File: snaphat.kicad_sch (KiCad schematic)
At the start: 98 parts, among them J1 Conn_01x08_S8B-PH-K-S(LF)(SN), J10 P70-6000045R, J11 P70-6000045R, J12 P70-6000045R, J2 Conn_02x20_2214SM-40G-75-PCR, J3 Conn_01x02_B2B-PH-K-S(LF)(SN), J4 USB_C_USB4930-00-A, J5 Conn_01x03_MC34747, J6 Conn_01x04_SFV4R-3STBE1HLF/C, J7 Conn_01x04_SFV4R-3STBE1HLF/C, J8 P70-6000045R, J9 P70-6000045R, Q1 Q_BC817-25, SW1 SW_B3FS-1050, SW2 SW_B3FS-1050, SW3 SW_B3FS-1050, SW4 SW_B3FS-1050, SW5 SW_B3FS-1050, SW6 SW_B3FS-1050, SW7 SW_B3FS-1050, SW8 SW_B3F-3150, U6 LIS2DW12TR

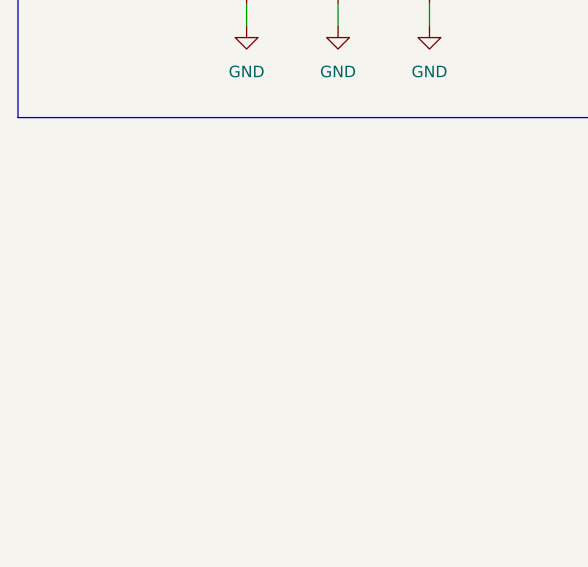
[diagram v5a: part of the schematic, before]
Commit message: Layout nits, add proper mounting holes
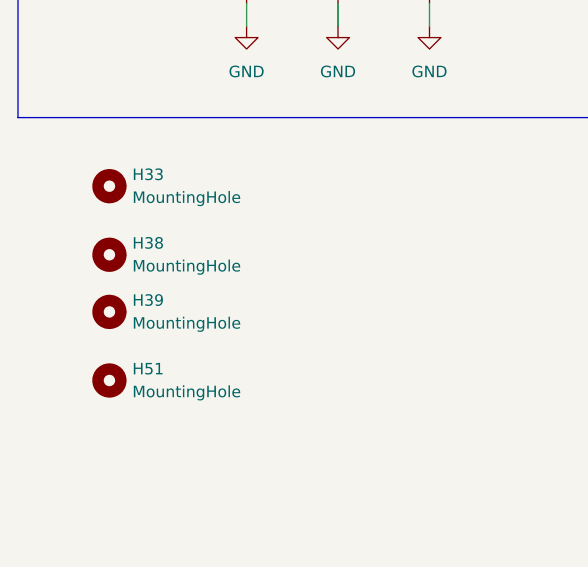
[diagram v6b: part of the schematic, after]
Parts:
- added H33, H38, H39, H51: MountingHole, library:MountingHole_2.7mm, symbol library:MountingHole
- J1: footprint library:DW08R -> library:JST_S8B-PH-K-S_LF__SN_

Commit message: Layout nits
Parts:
- added TP15, TP16, TP17: TestPoint, library:TestPoint_Pad_D1.5mm, symbol library:TestPoint
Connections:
- net GND_EXT: now also TP15.1
- net OTG_EXT: now also TP17.1
- net VBUS_EXT: now also TP16.1

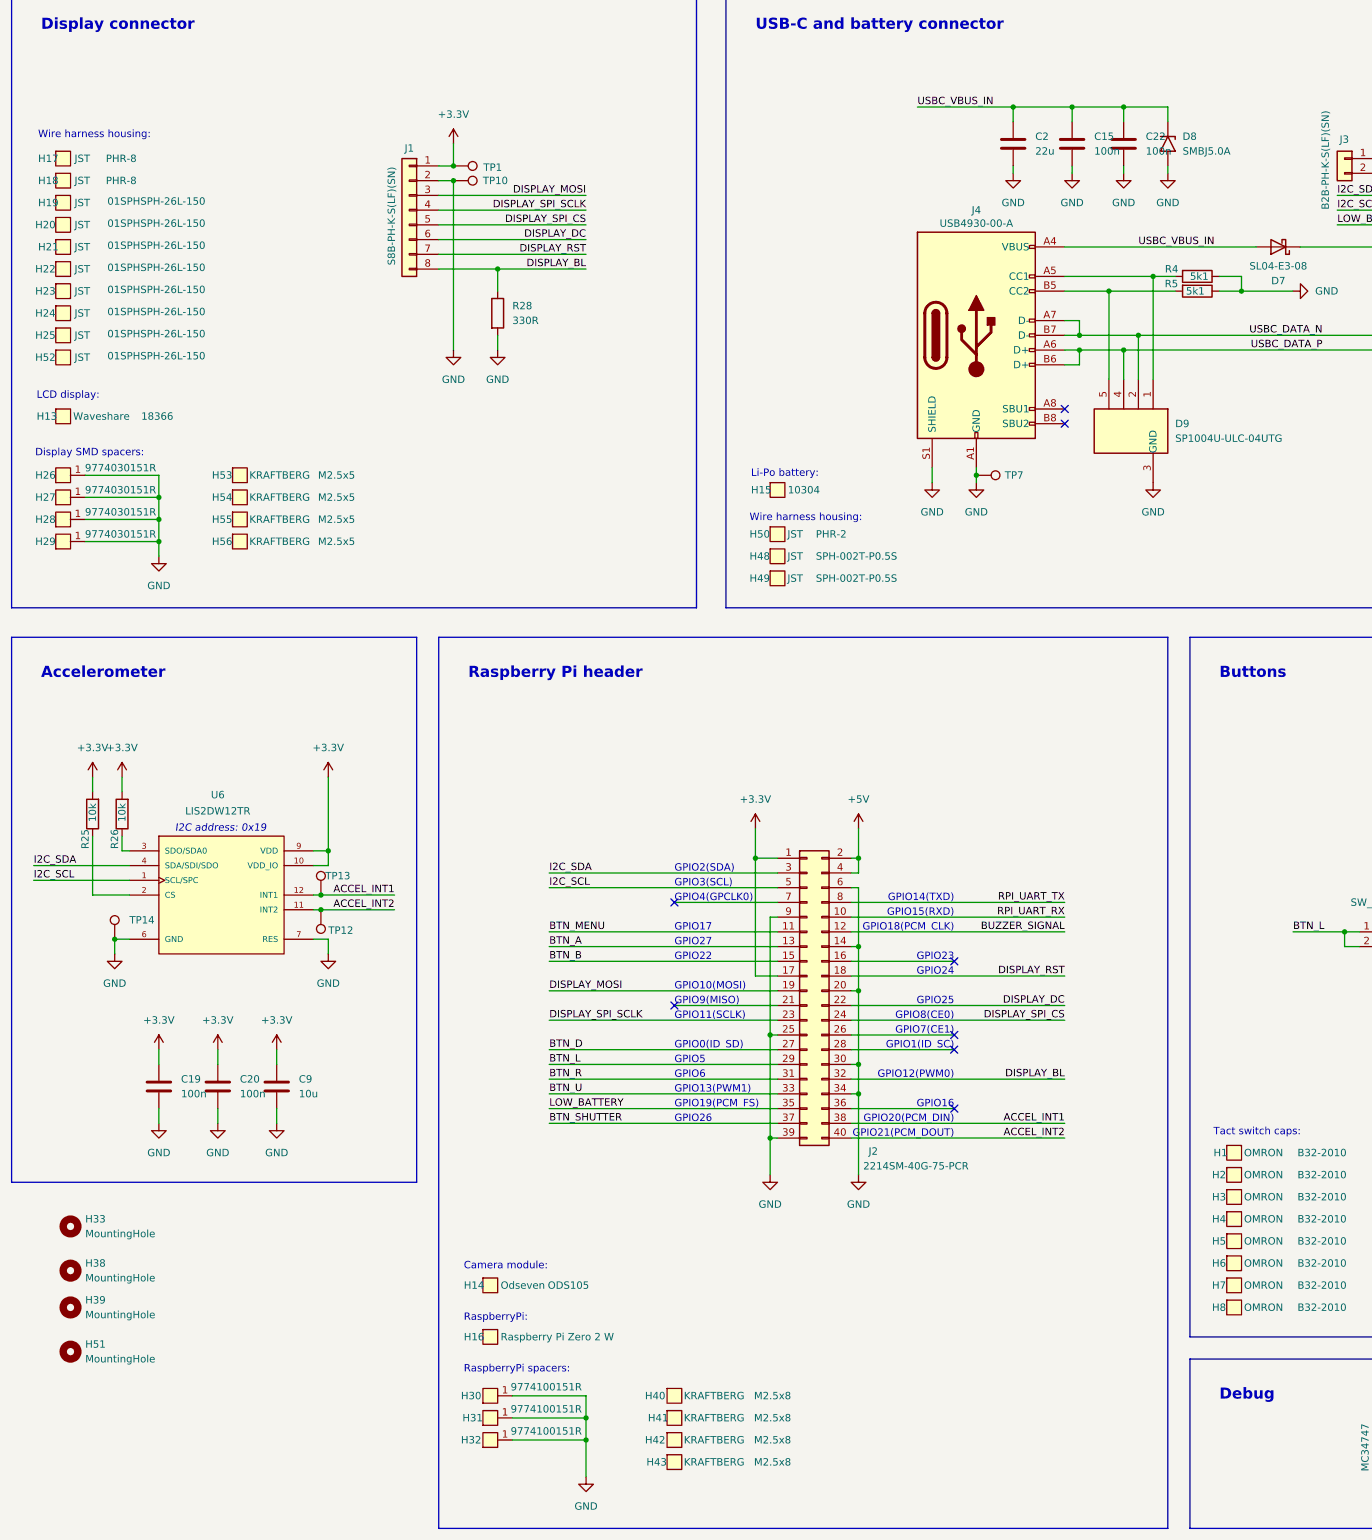
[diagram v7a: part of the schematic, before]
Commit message: Arrange designators, clear DRC, cleanups
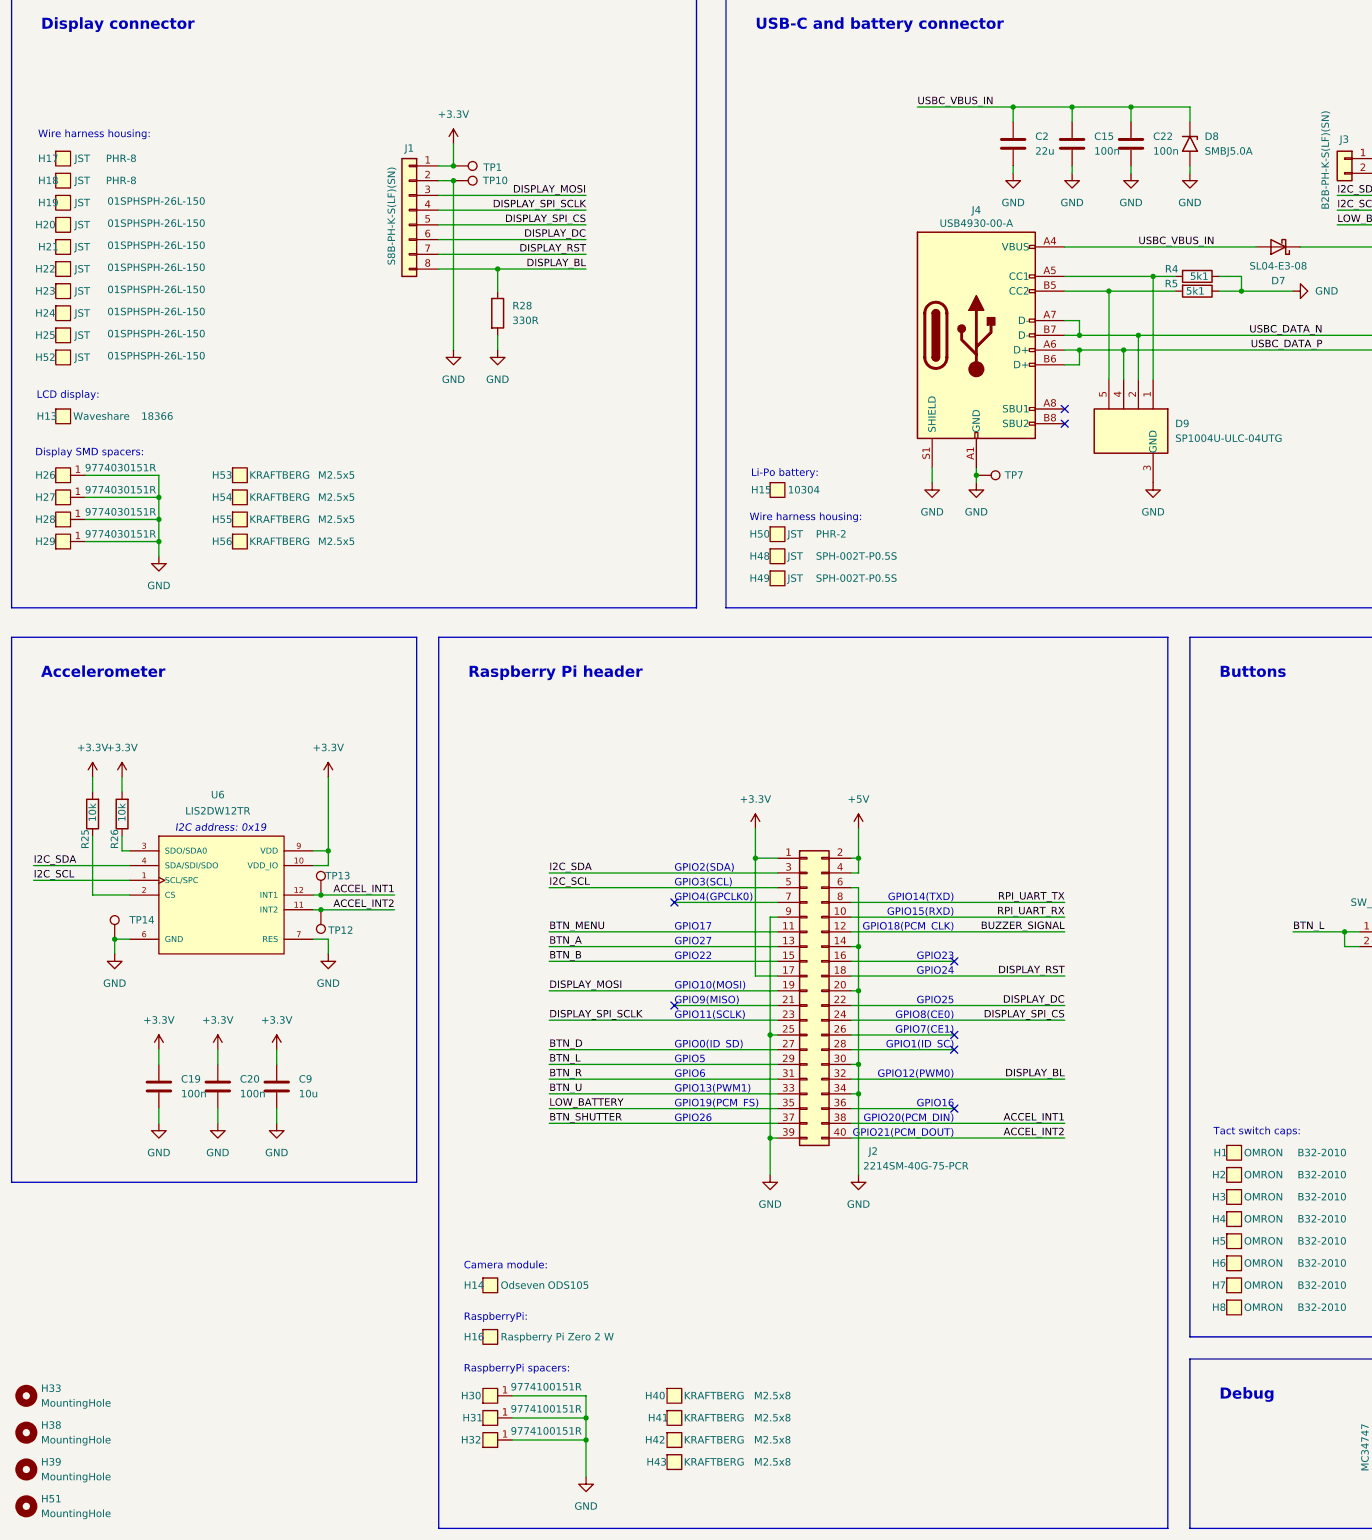
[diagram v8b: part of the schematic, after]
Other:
- moved on the sheet: C22, D8, H33, H38, H39, H51
